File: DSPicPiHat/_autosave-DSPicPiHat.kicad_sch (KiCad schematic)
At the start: 20 parts

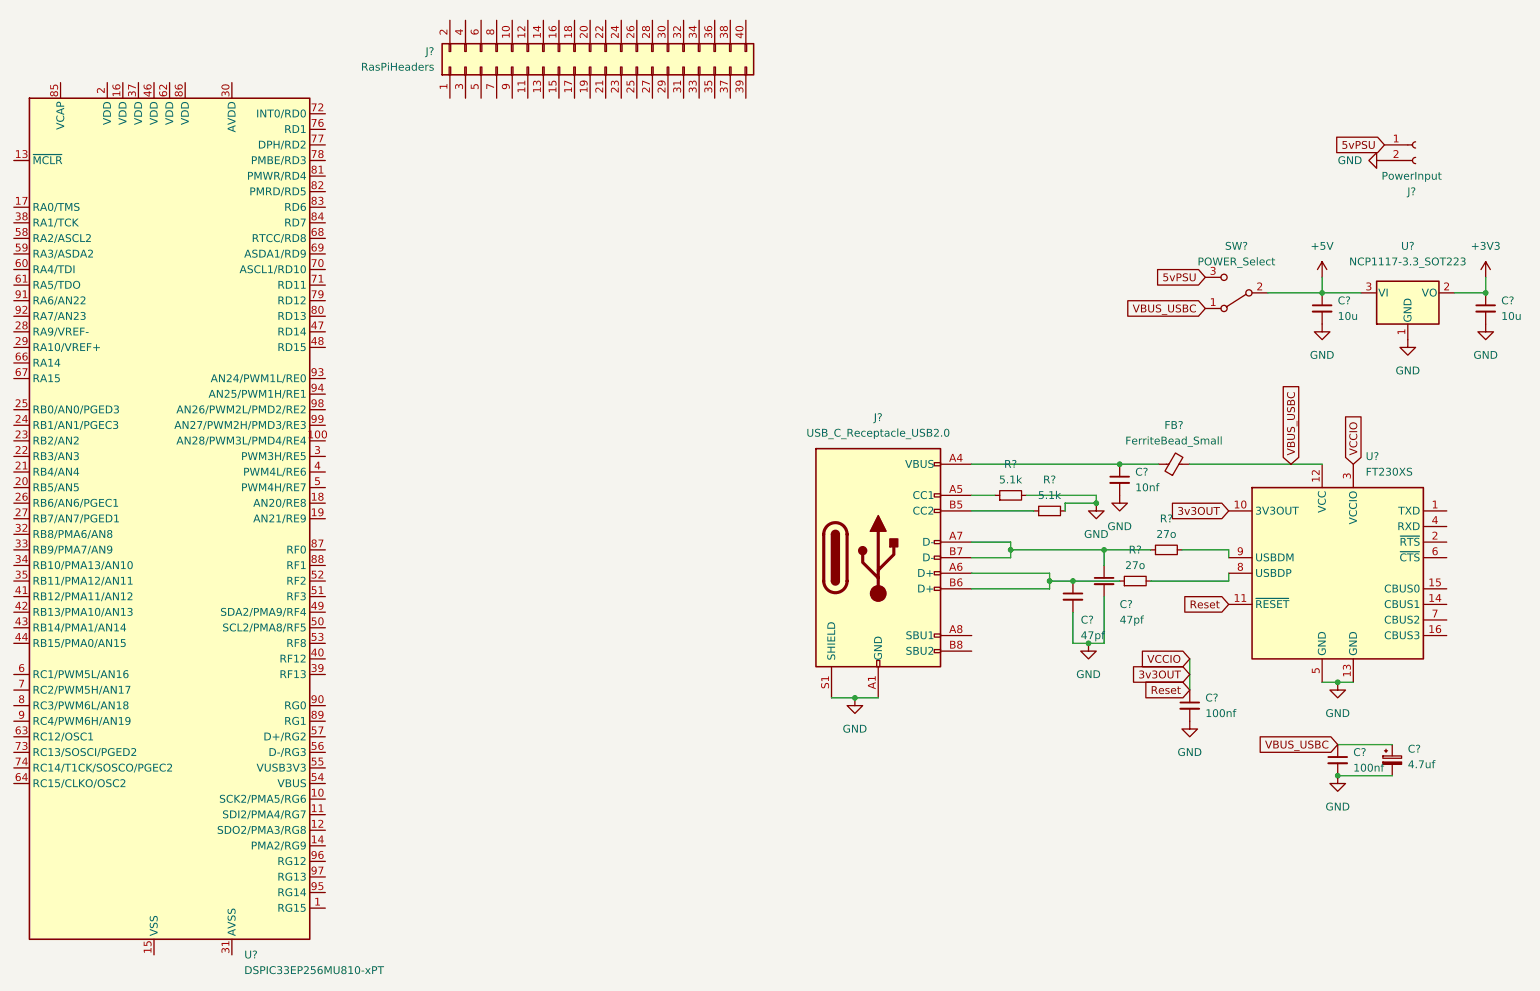
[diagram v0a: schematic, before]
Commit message: Added linear regulator expanded to-do list
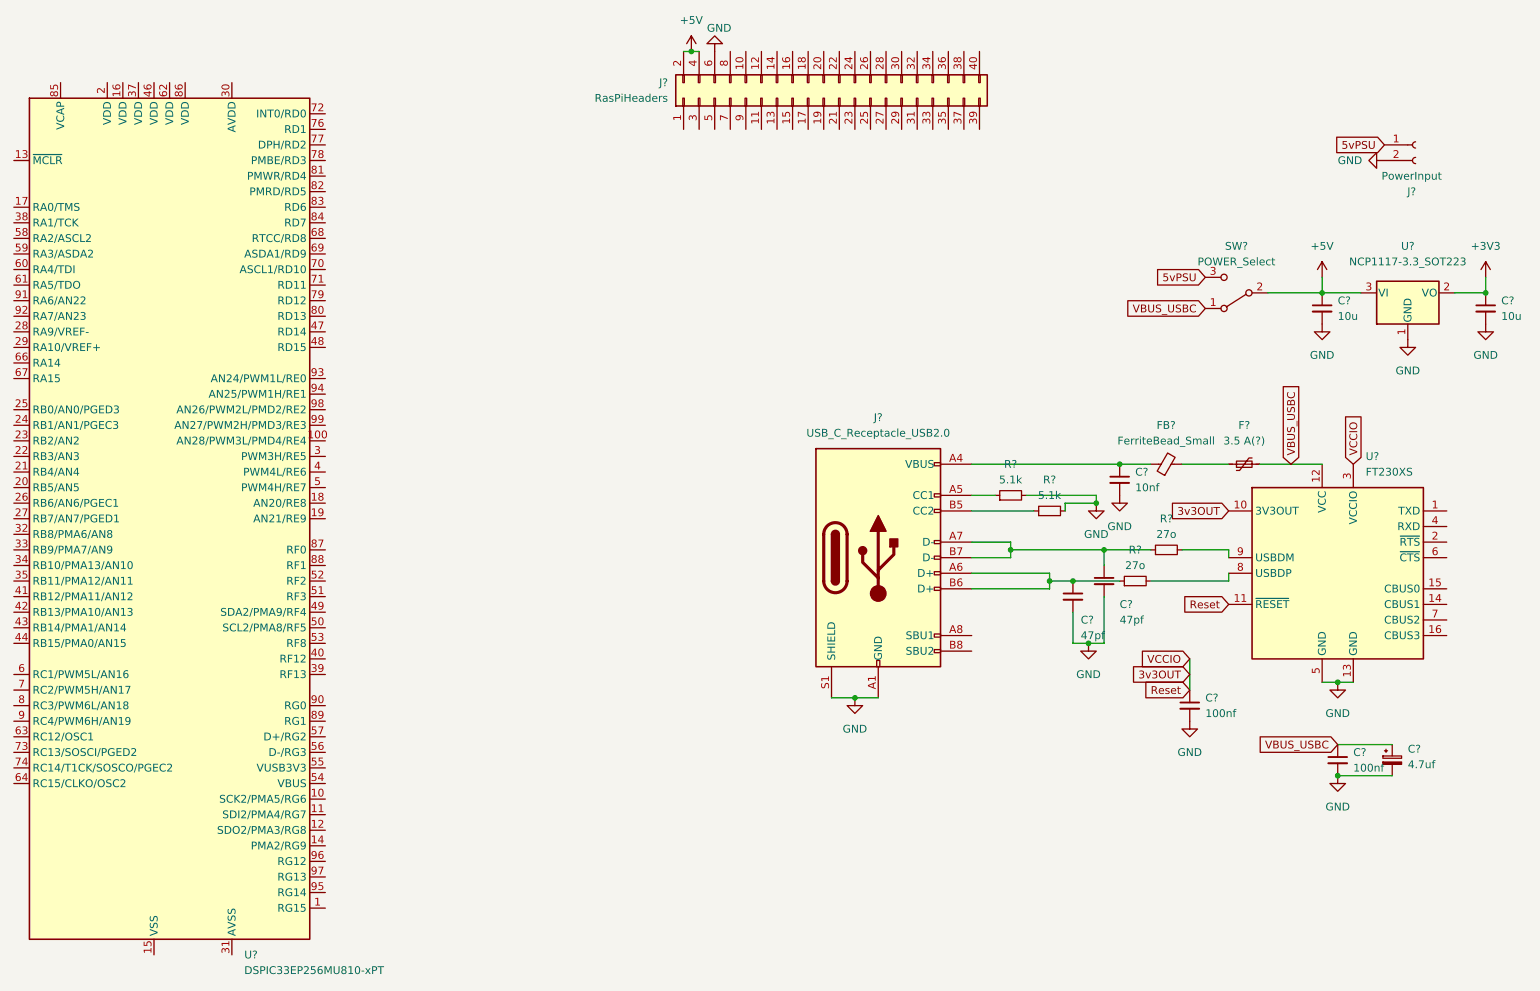
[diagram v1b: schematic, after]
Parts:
- added F?: 3.5 A(?), symbol Device:Polyfuse_Small
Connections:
- net +5V: now also J?.2 (Pin_2), J?.4 (Pin_4)
- net GND: now also J?.6 (Pin_6)
- net VBUS_USBC: now also F?.2; no longer FB?.2
- new net: F?.1, FB?.2
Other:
- moved on the sheet: FB?, J?
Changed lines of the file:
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@@
   (junction (at 278.13 68.58) (diameter 0) (color 0 0 0 0)
   )
+  (junction (at 148.59 29.21) (diameter 0) (color 0 0 0 0)
+  )
   (wire (pts (xy 203.2 101.6) (xy 214.63 101.6))
     (stroke (width 0) (type default) (color 0 0 0 0))
@@
     (stroke (width 0) (type default) (color 0 0 0 0))
   )
+  (wire (pts (xy 241.3 96.52) (xy 251.46 96.52))
+    (stroke (width 0) (type default) (color 0 0 0 0))
+  )
   (wire (pts (xy 194.31 104.14) (xy 204.47 104.14))
     (stroke (width 0) (type default) (color 0 0 0 0))
@@
     (stroke (width 0) (type default) (color 0 0 0 0))
   )
-  (wire (pts (xy 218.44 96.52) (xy 224.79 96.52))
+  (wire (pts (xy 218.44 96.52) (xy 223.52 96.52))
     (stroke (width 0) (type default) (color 0 0 0 0))
   )
@@
     (stroke (width 0) (type default) (color 0 0 0 0))
   )
-  (wire (pts (xy 229.87 96.52) (xy 251.46 96.52))
+  (wire (pts (xy 228.6 96.52) (xy 236.22 96.52))
     (stroke (width 0) (type default) (color 0 0 0 0))
   )
@@
     (stroke (width 0) (type default) (color 0 0 0 0))
   )
+  (wire (pts (xy 148.59 29.21) (xy 149.86 29.21))
+    (stroke (width 0) (type default) (color 0 0 0 0))
+  )
   (wire (pts (xy 194.31 109.22) (xy 200.66 109.22))
     (stroke (width 0) (type default) (color 0 0 0 0))
   )
   (wire (pts (xy 236.22 115.57) (xy 223.52 115.57))
+    (stroke (width 0) (type default) (color 0 0 0 0))
+  )
+  (wire (pts (xy 148.59 29.21) (xy 147.32 29.21))
     (stroke (width 0) (type default) (color 0 0 0 0))
   )
@@
     (pin "1")
   )
-  (symbol (lib_id "Connector_Generic:Conn_02x20_Odd_Even") (at 132.08 31.75 90) (unit 1)
-    (in_bom yes) (on_board yes) (fields_autoplaced)
-    (property "Reference" "J?" (id 0) (at 106.68 29.2099 90)
-      (effects (font (size 1.27 1.27)) (justify left))
-    )
-    (property "Value" "RasPiHeaders" (id 1) (at 106.68 31.7499 90)
-      (effects (font (size 1.27 1.27)) (justify left))
-    )
-    (property "Footprint" "" (id 2) (at 132.08 31.75 0)
-      (effects (font (size 1.27 1.27)) hide)
-    )
-    (property "Datasheet" "~" (id 3) (at 132.08 31.75 0)
+  (symbol (lib_id "Connector_Generic:Conn_02x20_Odd_Even") (at 170.18 36.83 90) (unit 1)
+    (in_bom yes) (on_board yes) (fields_autoplaced)
+    (property "Reference" "J?" (id 0) (at 144.78 34.2899 90)
+      (effects (font (size 1.27 1.27)) (justify left))
+    )
+    (property "Value" "RasPiHeaders" (id 1) (at 144.78 36.8299 90)
+      (effects (font (size 1.27 1.27)) (justify left))
+    )
+    (property "Footprint" "" (id 2) (at 170.18 36.83 0)
+      (effects (font (size 1.27 1.27)) hide)
+    )
+    (property "Datasheet" "~" (id 3) (at 170.18 36.83 0)
       (effects (font (size 1.27 1.27)) hide)
     )
@@
     (pin "9")
   )
+  (symbol (lib_id "Device:Polyfuse_Small") (at 238.76 96.52 90) (unit 1)
+    (in_bom yes) (on_board yes) (fields_autoplaced)
+    (property "Reference" "F?" (id 0) (at 238.76 90.17 90))
+    (property "Value" "3.5 A(?)" (id 1) (at 238.76 92.71 90))
+    (property "Footprint" "" (id 2) (at 243.84 95.25 0)
+      (effects (font (size 1.27 1.27)) (justify left) hide)
+    )
+    (property "Datasheet" "~" (id 3) (at 238.76 96.52 0)
+      (effects (font (size 1.27 1.27)) hide)
+    )
+    (pin "1")
+    (pin "2")
+  )
   (symbol (lib_id "power:GND") (at 214.63 102.87 0) (unit 1)
     (in_bom yes) (on_board yes) (fields_autoplaced)
@@
     )
     (property "Datasheet" "" (id 3) (at 214.63 102.87 0)
+      (effects (font (size 1.27 1.27)) hide)
+    )
+    (pin "1")
+  )
+  (symbol (lib_id "power:+5V") (at 148.59 29.21 0) (unit 1)
+    (in_bom yes) (on_board yes)
+    (property "Reference" "#PWR?" (id 0) (at 148.59 33.02 0)
+      (effects (font (size 1.27 1.27)) hide)
+    )
+    (property "Value" "+5V" (id 1) (at 148.59 24.13 0))
+    (property "Footprint" "" (id 2) (at 148.59 29.21 0)
+      (effects (font (size 1.27 1.27)) hide)
+    )
+    (property "Datasheet" "" (id 3) (at 148.59 29.21 0)
       (effects (font (size 1.27 1.27)) hide)
     )
@@
     (pin "99")
   )
+  (symbol (lib_id "power:GND") (at 152.4 29.21 180) (unit 1)
+    (in_bom yes) (on_board yes)
+    (property "Reference" "#PWR?" (id 0) (at 152.4 22.86 0)
+      (effects (font (size 1.27 1.27)) hide)
+    )
+    (property "Value" "GND" (id 1) (at 151.13 25.4 0)
+      (effects (font (size 1.27 1.27)) (justify right))
+    )
+    (property "Footprint" "" (id 2) (at 152.4 29.21 0)
+      (effects (font (size 1.27 1.27)) hide)
+    )
+    (property "Datasheet" "" (id 3) (at 152.4 29.21 0)
+      (effects (font (size 1.27 1.27)) hide)
+    )
+    (pin "1")
+  )
   (symbol (lib_id "power:GND") (at 261.62 46.99 270) (unit 1)
     (in_bom yes) (on_board yes)
@@
     (pin "1")
   )
-  (symbol (lib_id "Device:FerriteBead_Small") (at 227.33 96.52 90) (unit 1)
-    (in_bom yes) (on_board yes) (fields_autoplaced)
-    (property "Reference" "FB?" (id 0) (at 227.2919 90.17 90))
-    (property "Value" "FerriteBead_Small" (id 1) (at 227.2919 92.71 90))
-    (property "Footprint" "" (id 2) (at 227.33 98.298 90)
-      (effects (font (size 1.27 1.27)) hide)
-    )
-    (property "Datasheet" "~" (id 3) (at 227.33 96.52 0)
+  (symbol (lib_id "Device:FerriteBead_Small") (at 226.06 96.52 90) (unit 1)
+    (in_bom yes) (on_board yes) (fields_autoplaced)
+    (property "Reference" "FB?" (id 0) (at 226.0219 90.17 90))
+    (property "Value" "FerriteBead_Small" (id 1) (at 226.0219 92.71 90))
+    (property "Footprint" "" (id 2) (at 226.06 98.298 90)
+      (effects (font (size 1.27 1.27)) hide)
+    )
+    (property "Datasheet" "~" (id 3) (at 226.06 96.52 0)
       (effects (font (size 1.27 1.27)) hide)
     )
@@
       (reference "#PWR?") (unit 1) (value "GND") (footprint "")
     )
+    (path "/190ec4ad-4b73-4e17-861e-6904cc730108"
+      (reference "#PWR?") (unit 1) (value "+5V") (footprint "")
+    )
     (path "/2baf1a3c-2264-4eba-a229-88a817080df5"
       (reference "#PWR?") (unit 1) (value "+5V") (footprint "")
     )
+    (path "/4f74e748-187a-4676-b8e7-e02e94b5c11c"
+      (reference "#PWR?") (unit 1) (value "GND") (footprint "")
+    )
     (path "/50f0e911-e2b8-4213-bc7f-567662262621"
       (reference "#PWR?") (unit 1) (value "GND") (footprint "")
@@
       (reference "C?") (unit 1) (value "10nf") (footprint "")
     )
+    (path "/0b60c446-5161-421b-a91b-bda5e4f17126"
+      (reference "F?") (unit 1) (value "3.5 A(?)") (footprint "")
+    )
     (path "/73568451-6492-491a-bea8-1d81af82b417"
